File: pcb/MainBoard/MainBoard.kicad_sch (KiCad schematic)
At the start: 11 parts

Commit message: pcb progress
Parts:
- gave numbers to parts that had none: 11
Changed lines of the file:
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@@
 		(on_board yes)
 		(dnp no)
-		(property "Reference" "R?"
+		(property "Reference" "R103"
 			(at 166.878 138.43 90)
 			(effects
@@
 			(project "MainBoard"
 				(path "/ac576ee3-ac6f-4244-babf-9af36c7a7db3"
-					(reference "R?")
+					(reference "R103")
 					(unit 1)
 				)
@@
 		(dnp no)
 		(fields_autoplaced yes)
-		(property "Reference" "SW?"
+		(property "Reference" "SW102"
 			(at 77.47 113.03 0)
 			(effects
@@
 			(project "MainBoard"
 				(path "/ac576ee3-ac6f-4244-babf-9af36c7a7db3"
-					(reference "SW?")
+					(reference "SW102")
 					(unit 1)
 				)
@@
 		(dnp no)
 		(fields_autoplaced yes)
-		(property "Reference" "SW?"
+		(property "Reference" "SW101"
 			(at 72.39 77.47 0)
 			(effects
@@
 			(project "MainBoard"
 				(path "/ac576ee3-ac6f-4244-babf-9af36c7a7db3"
-					(reference "SW?")
+					(reference "SW101")
 					(unit 1)
 				)
@@
 		(dnp yes)
 		(fields_autoplaced yes)
-		(property "Reference" "C?"
+		(property "Reference" "C104"
 			(at 204.47 153.6699 0)
 			(effects
@@
 			(project "MainBoard"
 				(path "/ac576ee3-ac6f-4244-babf-9af36c7a7db3"
-					(reference "C?")
+					(reference "C104")
 					(unit 1)
 				)
@@
 		(dnp no)
 		(fields_autoplaced yes)
-		(property "Reference" "#PWR050"
+		(property "Reference" "#PWR0102"
 			(at 184.15 31.75 0)
 			(effects
@@
 			(project "MainBoard"
 				(path "/ac576ee3-ac6f-4244-babf-9af36c7a7db3"
-					(reference "#PWR050")
+					(reference "#PWR0102")
 					(unit 1)
 				)
@@
 		(dnp no)
 		(fields_autoplaced yes)
-		(property "Reference" "#PWR055"
+		(property "Reference" "#PWR0103"
 			(at 191.77 31.75 0)
 			(effects
@@
 			(project "MainBoard"
 				(path "/ac576ee3-ac6f-4244-babf-9af36c7a7db3"
-					(reference "#PWR055")
+					(reference "#PWR0103")
 					(unit 1)
 				)
@@
 		(on_board yes)
 		(dnp no)
-		(property "Reference" "R?"
+		(property "Reference" "R104"
 			(at 166.878 140.97 90)
 			(effects
@@
 			(project "MainBoard"
 				(path "/ac576ee3-ac6f-4244-babf-9af36c7a7db3"
-					(reference "R?")
+					(reference "R104")
 					(unit 1)
 				)
@@
 		(dnp yes)
 		(fields_autoplaced yes)
-		(property "Reference" "C?"
+		(property "Reference" "C101"
 			(at 177.8 153.6699 0)
 			(effects
@@
 			(project "MainBoard"
 				(path "/ac576ee3-ac6f-4244-babf-9af36c7a7db3"
-					(reference "C?")
+					(reference "C101")
 					(unit 1)
 				)
@@
 		(on_board yes)
 		(dnp no)
-		(property "Reference" "#PWR062"
+		(property "Reference" "#PWR0107"
 			(at 257.81 81.28 0)
 			(effects
@@
 			(project "MainBoard"
 				(path "/ac576ee3-ac6f-4244-babf-9af36c7a7db3"
-					(reference "#PWR062")
+					(reference "#PWR0107")
 					(unit 1)
 				)
@@
 		(on_board yes)
 		(dnp no)
-		(property "Reference" "R?"
+		(property "Reference" "R102"
 			(at 88.9 120.65 90)
 			(effects
@@
 			(project "MainBoard"
 				(path "/ac576ee3-ac6f-4244-babf-9af36c7a7db3"
-					(reference "R?")
+					(reference "R102")
 					(unit 1)
 				)
@@
 		(dnp no)
 		(fields_autoplaced yes)
-		(property "Reference" "#PWR061"
+		(property "Reference" "#PWR0104"
 			(at 262.89 60.96 0)
 			(effects
@@
 			(project "MainBoard"
 				(path "/ac576ee3-ac6f-4244-babf-9af36c7a7db3"
-					(reference "#PWR061")
+					(reference "#PWR0104")
 					(unit 1)
 				)
@@
 		(on_board yes)
 		(dnp no)
-		(property "Reference" "#PWR048"
+		(property "Reference" "#PWR0108"
 			(at 67.31 90.17 0)
 			(effects
@@
 			(project "MainBoard"
 				(path "/ac576ee3-ac6f-4244-babf-9af36c7a7db3"
-					(reference "#PWR048")
+					(reference "#PWR0108")
 					(unit 1)
 				)
@@
 		(on_board yes)
 		(dnp no)
-		(property "Reference" "#PWR059"
+		(property "Reference" "#PWR0109"
 			(at 72.39 125.73 0)
 			(effects
@@
 			(project "MainBoard"
 				(path "/ac576ee3-ac6f-4244-babf-9af36c7a7db3"
-					(reference "#PWR059")
+					(reference "#PWR0109")
 					(unit 1)
 				)
@@
 		(dnp yes)
 		(fields_autoplaced yes)
-		(property "Reference" "C?"
+		(property "Reference" "C102"
 			(at 186.69 153.6699 0)
 			(effects
@@
 			(project "MainBoard"
 				(path "/ac576ee3-ac6f-4244-babf-9af36c7a7db3"
-					(reference "C?")
+					(reference "C102")
 					(unit 1)
 				)
@@
 		(dnp yes)
 		(fields_autoplaced yes)
-		(property "Reference" "C?"
+		(property "Reference" "C103"
 			(at 195.58 153.6699 0)
 			(effects
@@
 			(project "MainBoard"
 				(path "/ac576ee3-ac6f-4244-babf-9af36c7a7db3"
-					(reference "C?")
+					(reference "C103")
 					(unit 1)
 				)
@@
 		(dnp no)
 		(fields_autoplaced yes)
-		(property "Reference" "#PWR060"
+		(property "Reference" "#PWR0105"
 			(at 269.24 60.96 0)
 			(effects
@@
 			(project "MainBoard"
 				(path "/ac576ee3-ac6f-4244-babf-9af36c7a7db3"
-					(reference "#PWR060")
+					(reference "#PWR0105")
 					(unit 1)
 				)
@@
 		(dnp no)
 		(fields_autoplaced yes)
-		(property "Reference" "#PWR056"
+		(property "Reference" "#PWR0106"
 			(at 128.27 68.58 0)
 			(effects
@@
 			(project "MainBoard"
 				(path "/ac576ee3-ac6f-4244-babf-9af36c7a7db3"
-					(reference "#PWR056")
+					(reference "#PWR0106")
 					(unit 1)
 				)
@@
 		(dnp no)
 		(fields_autoplaced yes)
-		(property "Reference" "J?"
+		(property "Reference" "J101"
 			(at 248.92 54.61 0)
 			(effects
@@
 			(project "MainBoard"
 				(path "/ac576ee3-ac6f-4244-babf-9af36c7a7db3"
-					(reference "J?")
+					(reference "J101")
 					(unit 1)
 				)
@@
 		(on_board yes)
 		(dnp no)
-		(property "Reference" "R?"
+		(property "Reference" "R101"
 			(at 83.82 85.09 90)
 			(effects
@@
 			(project "MainBoard"
 				(path "/ac576ee3-ac6f-4244-babf-9af36c7a7db3"
-					(reference "R?")
+					(reference "R101")
 					(unit 1)
 				)
@@
 		(dnp no)
 		(fields_autoplaced yes)
-		(property "Reference" "#PWR054"
+		(property "Reference" "#PWR0101"
 			(at 176.53 31.75 0)
 			(effects
@@
 			(project "MainBoard"
 				(path "/ac576ee3-ac6f-4244-babf-9af36c7a7db3"
-					(reference "#PWR054")
+					(reference "#PWR0101")
 					(unit 1)
 				)
@@
 		(on_board yes)
 		(dnp no)
-		(property "Reference" "#PWR047"
+		(property "Reference" "#PWR0110"
 			(at 187.96 168.91 0)
 			(effects
@@
 			(project "MainBoard"
 				(path "/ac576ee3-ac6f-4244-babf-9af36c7a7db3"
-					(reference "#PWR047")
-					(unit 1)
-				)
+					(reference "#PWR0110")
+					(unit 1)
+				)

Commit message: dump pcb
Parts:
- added C105, C106: 22u, Capacitor_SMD:C_0805_2012Metric, symbol Device:C
- added J102, J103, J104: Mechanical, Connector_PinHeader_2.54mm:PinHeader_1x02_P2.54mm_Vertical, symbol Connector_Generic:Conn_01x02
- added J105: DebugConn, Connector_PinSocket_2.54mm:PinSocket_1x05_P2.54mm_Horizontal, symbol Connector_Generic:Conn_01x05
- added JP101, JP102, JP103, JP104: SolderJumper_3_Open, led-matrix:SolderJumper-3_Open_RoundedPad_Smol, symbol Jumper:SolderJumper_3_Open
- added R105, R106: 2k2, Resistor_SMD:R_0402_1005Metric, symbol Device:R
- C101, C102, C103, C104: value C -> 1uf; footprint Capacitor_SMD:C_0603_1608Metric -> Capacitor_SMD:C_0402_1005Metric; LCSC (none) -> C52923; now fitted; now in the parts list
- J101: value Conn_02x05_Odd_Even -> DaughterConn; footprint Connector_PinHeader_2.00mm:PinHeader_2x05_P2.00mm_Vertical -> Connector_PinHeader_2.54mm:PinHeader_2x05_P2.54mm_Vertical
- R103, R104: value 100R -> 4k7; LCSC C25076 -> C25900
- SW101, SW102: value TS-1187A-B-A-B -> SW; footprint RadPie2040:TS-1187A-B-A-B -> Button_Switch_SMD:SW_SPST_B3U-3000P; LCSC C318884 -> (none); now left out of the parts list
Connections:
- net +3V3: now also J101.2 (Pin_2), C105.1; no longer J101.4 (Pin_4)
- net +5V: now also J101.1 (Pin_1), C106.1; no longer J101.2 (Pin_2)
- net 5V_sense: now also R105.2; no longer C103.1
- net CC1: no longer C101.1
- net CC1_F: now also C101.1
- net CC2: no longer C102.1
- net CC2_F: now also C102.1
- net COL_SER: now also JP103.3 (B)
- net COL_~{SRCLR}: now also JP104.3 (B)
- net GND: now also C105.2, C106.2, J102.1 (Pin_1), J102.2 (Pin_2), J103.1 (Pin_1), J103.2 (Pin_2), J104.1 (Pin_1), J104.2 (Pin_2), J105.2 (Pin_2)
- net GPIO11: now also J101.7 (Pin_7); no longer J101.9 (Pin_9)
- net GPIO12: now also J101.6 (Pin_6); no longer J101.7 (Pin_7)
- net GPIO14: now also J101.4 (Pin_4), JP101.3 (B); no longer J101.3 (Pin_3)
- net GPIO15: now also J101.3 (Pin_3), JP102.3 (B); no longer J101.1 (Pin_1)
- net GPIO9: now also J101.9 (Pin_9); no longer J101.6 (Pin_6)
- net Isense: now also R106.2; no longer C104.1
- net ROW_SER: now also JP103.2 (C)
- net ROW_~{SRCLR}: now also JP104.2 (C)
- net UART_RX: now also J105.5 (Pin_5)
- net UART_TX: now also J105.4 (Pin_4)
- net CS_SW: now reaches R102.2, SW102.2
- net RESET_SW: now reaches R101.2, SW101.2
- new net 5v_sense_F: C103.1, R105.1
- new net Isense_F: C104.1, R106.1
- new net ROW_SER_J: JP101.1 (A), JP103.1 (A)
- new net ROW_~{SRCLR}_J: JP102.1 (A), JP104.1 (A)
- new net SWCLK: J105.1 (Pin_1)
- new net SWD: J105.3 (Pin_3)
- new net rp2040/GPIO14: JP101.2 (C)
- new net rp2040/GPIO15: JP102.2 (C)
- no-connect marks 0 -> 2
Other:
- note added: "TODO: Select switch model"
- note added: "connections to the dauther board"
- note added: "debug"
- note added: "no space for proper M3 mounting hoes lol"
- moved on the sheet: J101, R103

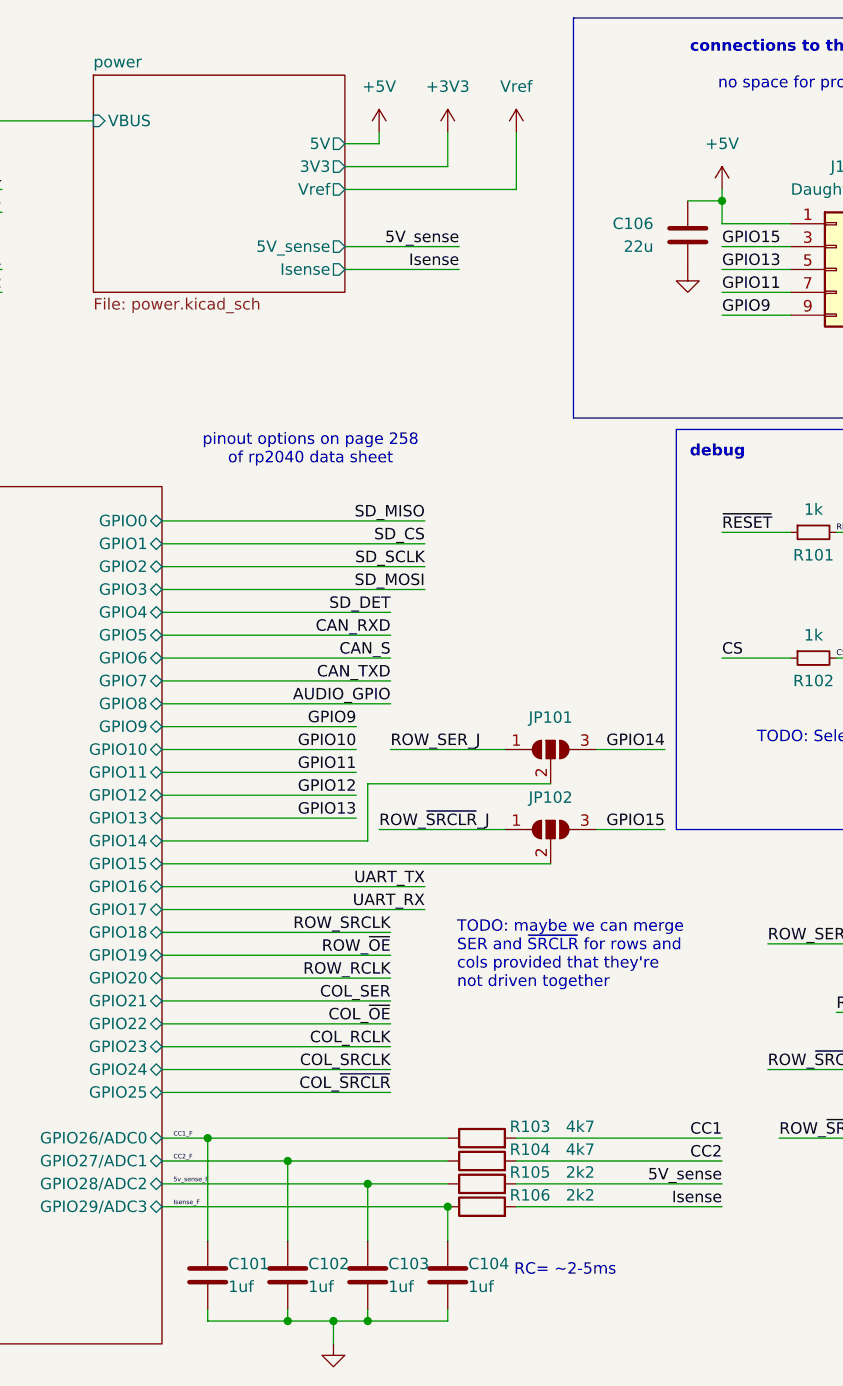
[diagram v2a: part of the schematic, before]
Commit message: MainBoard: fixes, simplify, BOM optimize, DRC fixes, ERC fixes
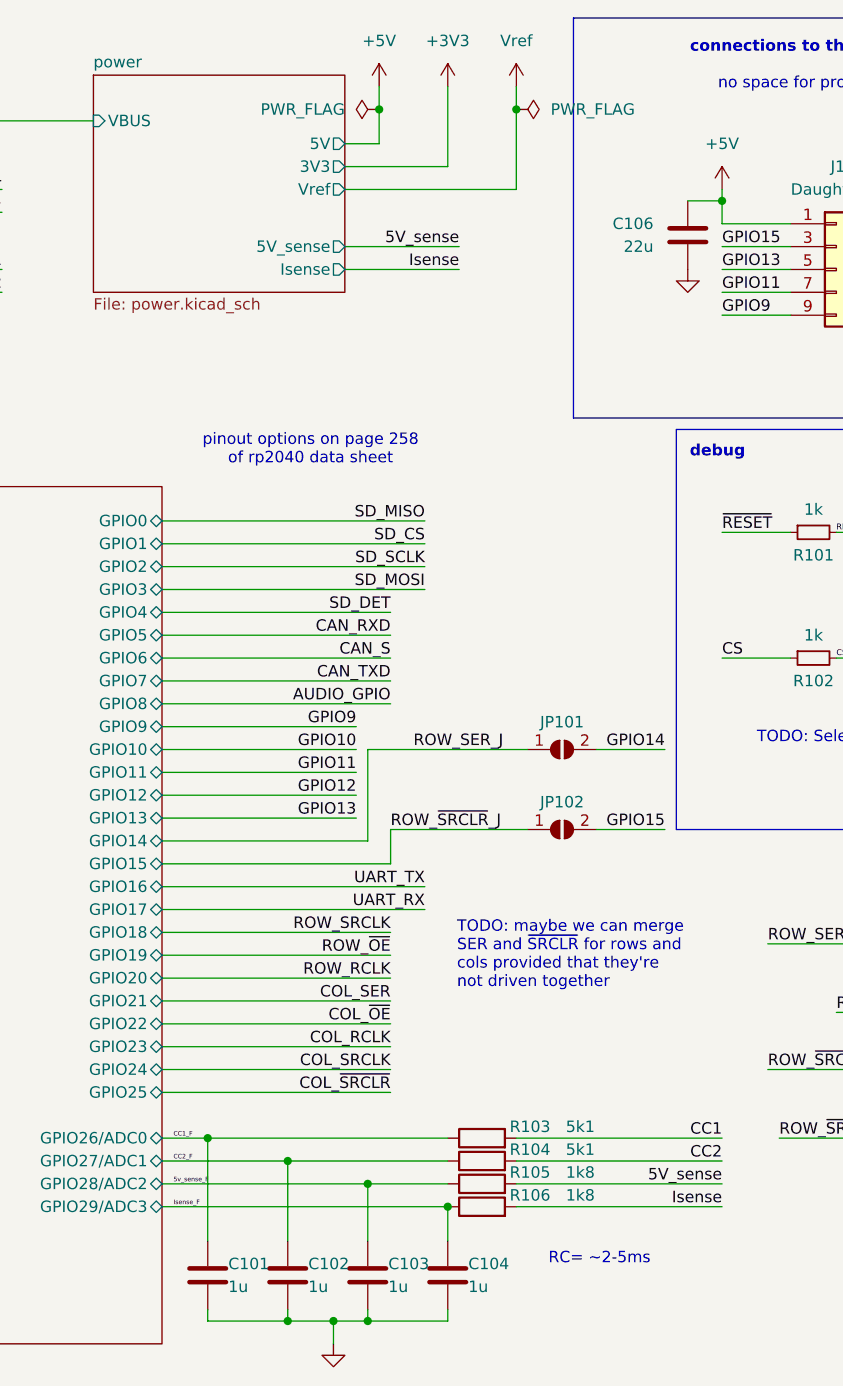
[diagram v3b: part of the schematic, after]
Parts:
- removed JP101, JP102: SolderJumper_3_Open, led-matrix:SolderJumper-3_Open_RoundedPad_Smol, symbol Jumper:SolderJumper_3_Open
- added JP101, JP102: SolderJumper_2_Open, led-matrix:SolderJumper-2_Open_RoundedPad_Smol, symbol Jumper:SolderJumper_2_Open
- C101, C102, C103, C104: value 1uf -> 1u
- J101, JP103, JP104: now left out of the parts list
- R103, R104: value 4k7 -> 5k1; LCSC C25900 -> C25905
- R105, R106: value 2k2 -> 1k8; footprint Resistor_SMD:R_0402_1005Metric -> Resistor_SMD:R_0603_1608Metric; LCSC C25879 -> C4177
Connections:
- net GPIO14: now also JP101.2 (B)
- net GPIO15: now also JP102.2 (B)
- net ROW_SER_J: now also JP101.1 (A)
- net ROW_~{SRCLR}_J: now also JP102.1 (A)

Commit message: pcb: fixes, improvements
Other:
- note added: "no space for proper M3 mounting holes"
- note removed: "no space for proper M3 mounting hoes lol"
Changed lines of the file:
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@@
 	)
 	(junction
-		(at 191.77 25.4)
+		(at 189.23 25.4)
 		(diameter 0)
 		(color 0 0 0 0)
@@
 	(wire
 		(pts
-			(xy 172.72 34.29) (xy 191.77 34.29)
+			(xy 172.72 34.29) (xy 189.23 34.29)
 		)
 		(stroke
@@
 	(wire
 		(pts
-			(xy 191.77 22.86) (xy 191.77 25.4)
+			(xy 189.23 22.86) (xy 189.23 25.4)
 		)
 		(stroke
@@
 	(wire
 		(pts
-			(xy 184.15 31.75) (xy 184.15 22.86)
+			(xy 182.88 31.75) (xy 182.88 22.86)
 		)
 		(stroke
@@
 	(wire
 		(pts
-			(xy 191.77 25.4) (xy 191.77 34.29)
+			(xy 189.23 25.4) (xy 189.23 34.29)
 		)
 		(stroke
@@
 	(wire
 		(pts
-			(xy 172.72 31.75) (xy 184.15 31.75)
+			(xy 172.72 31.75) (xy 182.88 31.75)
 		)
 		(stroke
@@
 	(wire
 		(pts
+			(xy 191.77 25.4) (xy 189.23 25.4)
+		)
+		(stroke
+			(width 0)
+			(type default)
+		)
+	)
+	(wire
+		(pts
 			(xy 121.92 43.18) (xy 134.62 43.18)
 		)
@@
 		)
 	)
-	(text_box "TODO: maybe we can merge SER and ~{SRCLR} for rows and cols provided that they're not driven together"
+	(text_box "maybe we can merge SER and ~{SRCLR} for rows and cols provided that they're not driven together\n\nTODO: can we also do that with ROW_OE?"
 		(exclude_from_sim no)
 		(at 184.15 114.3 0)
@@
 		)
 	)
-	(text "no space for proper M3 mounting hoes lol"
+	(text "no space for proper M3 mounting holes"
 		(exclude_from_sim no)
 		(at 232.41 22.606 0)
@@
 	(symbol
 		(lib_id "power:+3V3")
-		(at 184.15 22.86 0)
+		(at 182.88 22.86 0)
 		(unit 1)
 		(exclude_from_sim no)
@@
 		(fields_autoplaced yes)
 		(property "Reference" "#PWR0102"
-			(at 184.15 26.67 0)
+			(at 182.88 26.67 0)
 			(effects
 				(font
@@
 		)
 		(property "Value" "+3V3"
-			(at 184.15 17.78 0)
+			(at 182.88 17.78 0)
 			(effects
 				(font
@@
 		)
 		(property "Footprint" ""
-			(at 184.15 22.86 0)
+			(at 182.88 22.86 0)
 			(effects
 				(font
@@
 		)
 		(property "Datasheet" ""
-			(at 184.15 22.86 0)
+			(at 182.88 22.86 0)
 			(effects
 				(font
@@
 		)
 		(property "Description" "Power symbol creates a global label with name \"+3V3\""
-			(at 184.15 22.86 0)
+			(at 182.88 22.86 0)
 			(effects
 				(font
@@
 	(symbol
 		(lib_id "power:+3V3")
-		(at 191.77 22.86 0)
+		(at 189.23 22.86 0)
 		(unit 1)
 		(exclude_from_sim no)
@@
 		(fields_autoplaced yes)
 		(property "Reference" "#PWR0103"
-			(at 191.77 26.67 0)
+			(at 189.23 26.67 0)
 			(effects
 				(font
@@
 		)
 		(property "Value" "Vref"
-			(at 191.77 17.78 0)
+			(at 189.23 17.78 0)
 			(effects
 				(font
@@
 		)
 		(property "Footprint" ""
-			(at 191.77 22.86 0)
+			(at 189.23 22.86 0)
 			(effects
 				(font
@@
 		)
 		(property "Datasheet" ""
-			(at 191.77 22.86 0)
+			(at 189.23 22.86 0)
 			(effects
 				(font
@@
 		)
 		(property "Description" "Vref"
-			(at 191.77 22.86 0)
+			(at 189.23 22.86 0)
 			(effects
 				(font

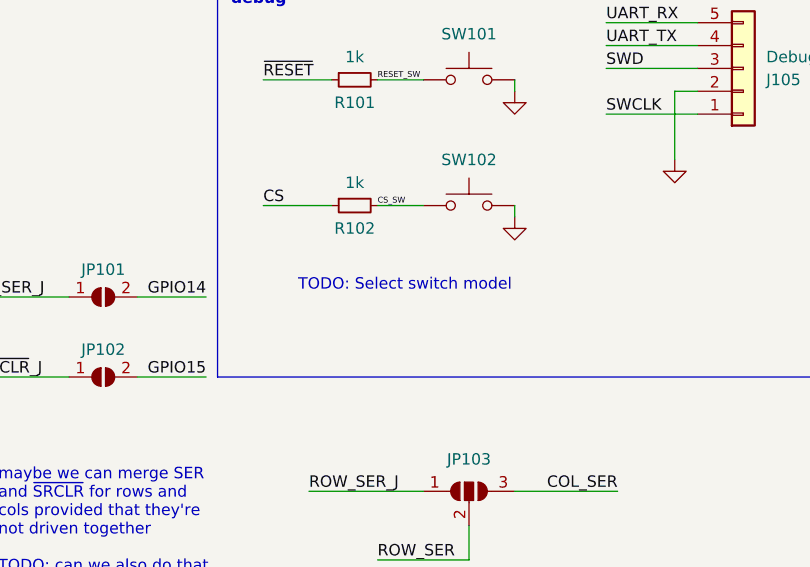
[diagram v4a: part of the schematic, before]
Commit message: pcb: add microswitches
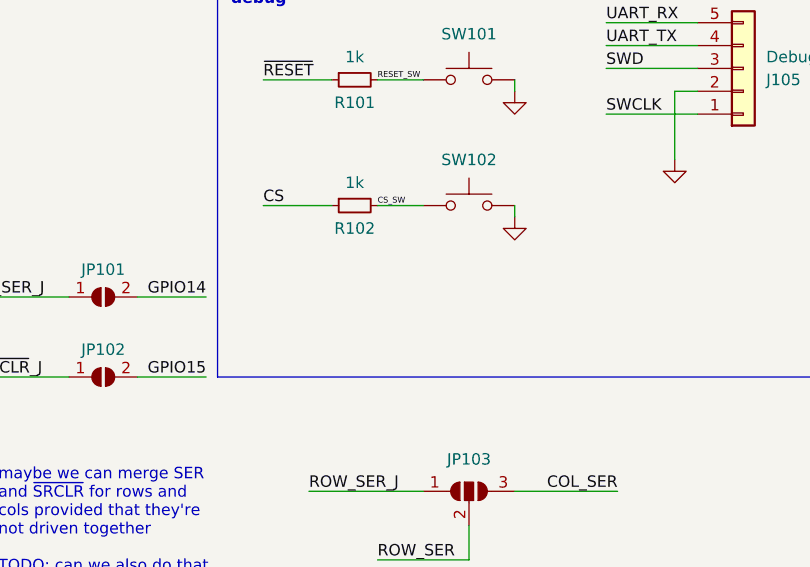
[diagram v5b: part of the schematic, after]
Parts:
- SW101, SW102: footprint Button_Switch_SMD:SW_SPST_B3U-3000P -> led-matrix:HY-C-03
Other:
- note removed: "TODO: Select switch model"
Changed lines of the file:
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@@
 		)
 	)
-	(text "TODO: Select switch model"
-		(exclude_from_sim no)
-		(at 230.378 95.25 0)
-		(effects
-			(font
-				(size 1.27 1.27)
-			)
-		)
-	)
 	(text "pinout options on page 258\nof rp2040 data sheet"
 		(exclude_from_sim no)
@@
 			)
 		)
-		(property "Footprint" "Button_Switch_SMD:SW_SPST_B3U-3000P"
+		(property "Footprint" "led-matrix:HY-C-03"
 			(at 237.49 67.31 0)
 			(effects
@@
 			)
 		)
-		(property "Footprint" "Button_Switch_SMD:SW_SPST_B3U-3000P"
+		(property "Footprint" "led-matrix:HY-C-03"
 			(at 237.49 81.28 0)
 			(effects
